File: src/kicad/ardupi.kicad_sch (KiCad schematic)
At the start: 60 parts

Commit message: +adc
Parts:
- removed U (x8): (no value), symbol Device:R_Small
- added J: 6_PIN_SERIAL_TARGET, 1X06, symbol SparkFun-Connectors:6_PIN_SERIAL_TARGET
- added U (x12): (no value), symbol Device:R_Small
- added U: (no value), symbol Device:C_Small
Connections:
- net GND: now also U.3 (GND), J.CTS (5), J.GND (6), U.1, U.1
- net PWM10: now also U.1
- net PWM11: now also U.1
- net PWM12: now also U.1
- net PWM13: now also U.1
- net PWM14: now also U.1
- net PWM15: now also U.1
- net PWM16: now also U.1
- net PWM9: now also U.1
- net at U.1: now also U.2 (x2)
- net at U.4: now also U.2 (x2)
- net at U.7: now also U.2 (x2)
- net at U.10: now also U.2
- net at U.1 (ADDR): now also U.2
- net at U.10 (SCL): now also U.1
- net at U.2 (ALERT/RDY): now also U.1
- net AIO0: now reaches U.4 (AIN0)
- net AIO0: now also J.VCC (4)
- net AIO1: now reaches U.5 (AIN1)
- net AIO1: now also J.TXO (3)
- net AIO2: now reaches U.6 (AIN2)
- net AIO2: now also J.RXI (2)
- net AIO3: now reaches U.7 (AIN3)
- net AIO3: now also J.DTR (1)
- net VDD: now reaches U.8 (VDD)
- net VDD: now also U.2, U.2, U.2
- net at U.9 (SDA): now also U.1
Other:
- note added: "ADC1"
- note added: "MPU9250"
- moved on the sheet: J, U

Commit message: fix
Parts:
- removed J (x3): CONN_04POLAR, MOLEX-1X4, symbol SparkFun-Connectors:CONN_04POLAR
- removed J: 6_PIN_SERIAL_TARGET, 1X06, symbol SparkFun-Connectors:6_PIN_SERIAL_TARGET
- removed J: Conn_01x10, symbol Connector_Generic:Conn_01x10
- removed J: CONN_06POLAR, MOLEX-1X6, symbol SparkFun-Connectors:CONN_06POLAR
- removed J: CONN_02POLAR, MOLEX-1X2, symbol SparkFun-Connectors:CONN_02POLAR
- removed J: CONN_05, 1X05, symbol SparkFun-Connectors:CONN_05
- removed U (x4): (no value), symbol Adafruit PCA9685 rev C-eagle-import:HEADER-3X04
- removed U (x22): (no value), symbol Device:R_Small
- removed U: (no value), symbol Device:C_Small
- added C?: 10uF, Capacitor_SMD:C_0402_1005Metric, symbol Device:C_Small
- added J?: Conn_01x02, Connector_JST:JST_EH_B2B-EH-A_1x02_P2.50mm_Vertical, symbol Connector_Generic:Conn_01x02
- added J?: Conn_01x04, symbol Connector_Generic:Conn_01x04
- added J?: Conn_01x06, symbol Connector_Generic:Conn_01x06
- added J? (x2): Conn_01x04, Connector_JST:JST_EH_B4B-EH-A_1x04_P2.50mm_Vertical, symbol Connector_Generic:Conn_01x04
- added J?: Conn_01x05, Connector_JST:JST_EH_B5B-EH-A_1x05_P2.50mm_Vertical, symbol Connector_Generic:Conn_01x05
- added J?: Conn_01x10, symbol Connector_Generic:Conn_01x10
- added J?: Conn_01x05, symbol Connector_Generic:Conn_01x05
- added JP? (x4): PWM-HEADER-3X04, Ardupi:PWM-Header-3x4, symbol Ardupi:PWM-HEADER-3X04
- added R? (x16): 220 Ω, Resistor_SMD:R_0402_1005Metric, symbol Device:R_Small
- added R? (x4): 10KΩ, Resistor_SMD:R_0402_1005Metric, symbol Device:R_Small
- added R? (x2): 470k, Resistor_SMD:R_0402_1005Metric, symbol Device:R_Small
- BMP280: renamed from U; value (none) -> BMP280; footprint (none) -> Package_LGA:Bosch_LGA-8_2x2.5mm_P0.65mm_ClockwisePinNumbering
- C1, C3: renamed from U; value (none) -> 0.1uF; footprint (none) -> Capacitor_SMD:C_0402_1005Metric
- C2, C5: renamed from U; value (none) -> 1uF; footprint (none) -> Capacitor_SMD:C_0402_1005Metric
- C4: renamed from U; value (none) -> 0.01uF; footprint (none) -> Capacitor_SMD:C_0402_1005Metric
- C_PCA1: renamed from U; value (none) -> 10uF; footprint (none) -> Capacitor_SMD:CP_Elec_8x5.4
- H1, H2, H3, H4: renamed from U; value (none) -> MountingHole; footprint (none) -> lib:MountingHole_2.7mm_M2.5_uHAT_RPi
- J1: renamed from U; value (none) -> GPIO_CONNECTOR; footprint (none) -> lib:PinSocket_2x20_P2.54mm_Vertical_Centered_Anchor
- R1, R3, R4, R5: renamed from U; value (none) -> 10K; footprint (none) -> Resistor_SMD:R_0402_1005Metric
- R2, R6, R7: renamed from U; value (none) -> 10k; footprint (none) -> Resistor_SMD:R_0402_1005Metric
- R24, R25, R27, R29, R30: renamed from U; value (none) -> 4.7KΩ; footprint (none) -> Resistor_SMD:R_0402_1005Metric
- R26, R28, R31: renamed from U; value (none) -> 10KΩ; footprint (none) -> Resistor_SMD:R_0402_1005Metric
- U1: renamed from U; value (none) -> MPU-9250; footprint (none) -> Sensor_Motion:InvenSense_QFN-24_3x3mm_P0.4mm
- U2: renamed from U; value (none) -> ULN2803ADW; footprint (none) -> uln2803ADW:ULN2803ADW
- U4: renamed from U; value (none) -> PCA9685BS; footprint (none) -> Package_DFN_QFN:QFN-28-1EP_6x6mm_P0.65mm_EP4.25x4.25mm
- U6: renamed from U; value (none) -> ADS1115IRUGR; footprint (none) -> ADS1115IRUGR:ADS1115IRUGR
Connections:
- net +5V: now also J?.1 (Pin_1), J?.1 (Pin_1), J?.1 (Pin_1), J?.2 (Pin_2), J?.2 (Pin_2), JP?.11, JP?.11, JP?.11, JP?.11, JP?.2, JP?.2, JP?.2, JP?.2, JP?.5, JP?.5, JP?.5, JP?.5, JP?.8, JP?.8, JP?.8, JP?.8, R?.1
- net AIO0: now also J?.4 (Pin_4); no longer U6.4 (AIN0)
- net AIO1: now also U6.4 (AIN0), J?.3 (Pin_3); no longer U6.5 (AIN1)
- net AIO2: now also U6.5 (AIN1), J?.2 (Pin_2); no longer U6.6 (AIN2)
- net AIO3: now also U6.6 (AIN2), J?.1 (Pin_1)
- net BUZZER_OUT: now also J?.1 (Pin_1)
- net GND: now also C?.2, J?.1 (Pin_1), J?.1 (Pin_1), J?.2 (Pin_2), J?.4 (Pin_4), J?.4 (Pin_4), J?.5 (Pin_5), J?.6 (Pin_6), JP?.12, JP?.12, JP?.12, JP?.12, JP?.3, JP?.3, JP?.3, JP?.3, JP?.6, JP?.6, JP?.6, JP?.6, JP?.9, JP?.9, JP?.9, JP?.9, R?.1
- net MISO: now also J?.4 (Pin_4)
- net MOSI: now also J?.3 (Pin_3)
- net PCA_EN: now also R?.1
- net PWM1: now also R?.2
- net PWM10: now also R?.2
- net PWM11: now also R?.2
- net PWM12: now also R?.2
- net PWM13: now also R?.2
- net PWM14: now also R?.2
- net PWM15: now also R?.2
- net PWM16: now also R?.2
- net PWM2: now also R?.2
- net PWM3: now also R?.2
- net PWM4: now also R?.2
- net PWM5: now also R?.2
- net PWM6: now also R?.2
- net PWM7: now also R?.2
- net PWM8: now also R?.2
- net PWM9: now also R?.2
- net RC1: now also J?.3 (Pin_3)
- net RC2: now also J?.4 (Pin_4)
- net RC3: now also J?.5 (Pin_5)
- net RC4: now also J?.6 (Pin_6)
- net RC5: now also J?.7 (Pin_7)
- net RC6: now also J?.8 (Pin_8)
- net RC7: now also J?.9 (Pin_9)
- net RC8: now also J?.10 (Pin_10)
- net RX: now also J?.4 (Pin_4)
- net SCL: now also J?.3 (Pin_3), J?.3 (Pin_3)
- net SCLK: now also J?.5 (Pin_5)
- net SDA: now also J?.2 (Pin_2), J?.2 (Pin_2)
- net SRVO_EN: now also J?.1 (Pin_1)
- net TX: now also J?.3 (Pin_3)
- net VDD: now also R?.2, R?.2, R?.2; no longer U6.8 (VDD)
- net V_EXT: now also J?.5 (Pin_5)
- net at U6.1 (ADDR): now also R?.2
- net at U6.9 (SDA): now also R?.1
- net at U6.2 (ALERT/RDY): now also R?.1
- net at U6.10 (SCL): now also R?.1
- net LED_1 renamed LED1
- net LED_1_OUT renamed LED1_OUT
- net LED1_OUT: now also J?.2 (Pin_2)
- net LED_2 renamed LED2
- net LED_2_OUT renamed LED2_OUT
- net LED2_OUT: now also J?.3 (Pin_3)
- net LED_3 renamed LED3
- net LED_3_OUT renamed LED3_OUT
- net LED3_OUT: now also J?.4 (Pin_4)
- new net: J?.2 (Pin_2), R?.2, R?.2
- new net: JP?.1, R?.1 (x4)
- new net: JP?.10, R?.1 (x4)
- new net: JP?.7, R?.1 (x4)
- new net: JP?.4, R?.1 (x4)
- new net: C?.1, U6.8 (VDD)
- no-connect marks 29 -> 28
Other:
- note added: "ADC"
- note added: "I2C"
- note added: "RC"
- note added: "SERIAL"
- note added: "SPI"
- note removed: "ADC1"
- note removed: "I2C1"
- note removed: "RC In"
- note removed: "SPI1"
- note removed: "Serial1"
- moved on the sheet: C1, C2, C3, C4, C5, C_PCA1, J1, R1, R2, U1, U2, U4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

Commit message: clean layout
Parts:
- removed JP? (x2): PWM-HEADER-3X04, Ardupi:PWM-Header-3x4, symbol Ardupi:PWM-HEADER-3X04
- removed R? (x8): 220 Ω, Resistor_SMD:R_0402_1005Metric, symbol Device:R_Small
- J2: renamed from J?; footprint (none) -> Connector_JST:JST_EH_B10B-EH-A_1x10_P2.50mm_Vertical
- J3: renamed from J?; footprint (none) -> Connector_JST:JST_EH_B5B-EH-A_1x05_P2.50mm_Vertical
- J4: renamed from J?; footprint (none) -> Connector_JST:JST_EH_B4B-EH-A_1x04_P2.50mm_Vertical
- J6: renamed from J?; footprint (none) -> Connector_JST:JST_EH_B6B-EH-A_1x06_P2.50mm_Vertical
- U6: footprint ADS1115IRUGR:ADS1115IRUGR -> Ardupi:ADS1115IRUGR
- gave numbers to parts that had none: 21
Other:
- moved on the sheet: BMP280, C1, C2, C3, C4, C5, C6, C_PCA1, JP1, JP2, R1, R2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

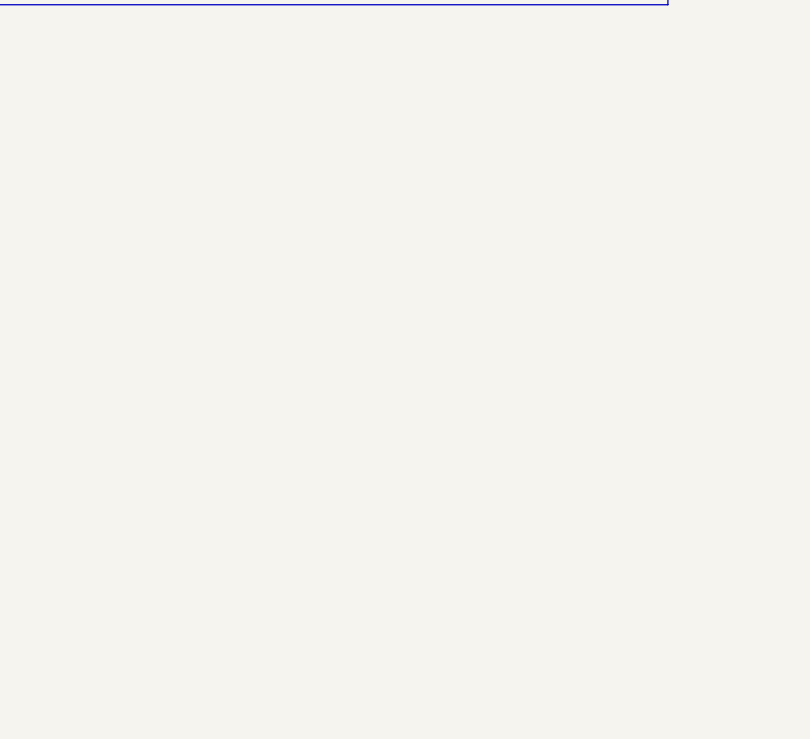
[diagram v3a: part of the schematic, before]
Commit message: +3x8 PWM header
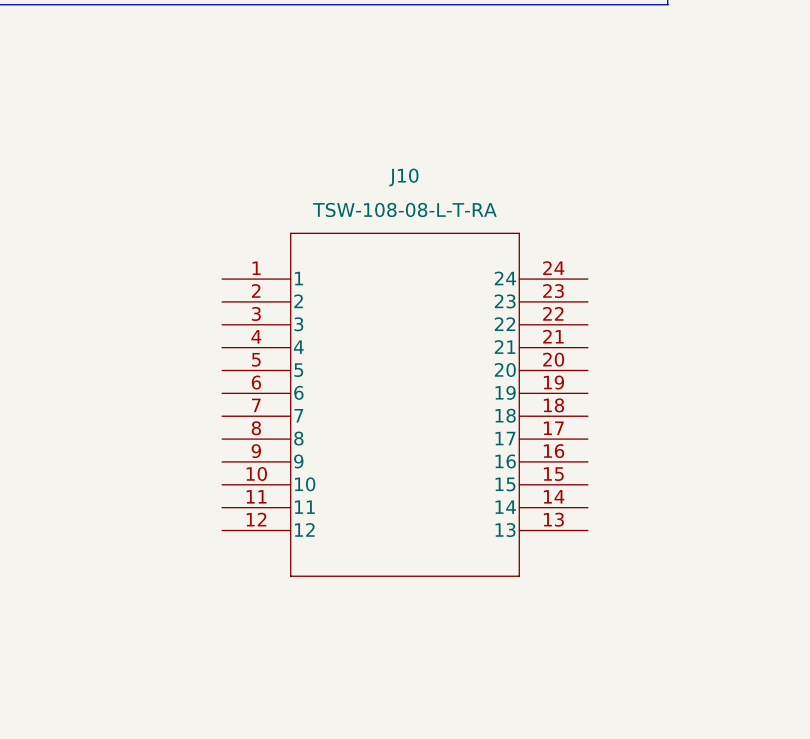
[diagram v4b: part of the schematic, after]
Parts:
- added J10: TSW-108-08-L-T-RA, Ardupi:TSW-108-08-L-T-RA, symbol Ardupi:TSW-108-08-L-T-RA

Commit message: elec: ADS1115
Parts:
- removed R34: 10KΩ, Resistor_SMD:R_0402_1005Metric, symbol Device:R_Small
- added C?: 0.1uf, Capacitor_SMD:C_0402_1005Metric, symbol Device:C_Small
- added R?: 10KΩ, Resistor_SMD:R_0402_1005Metric, symbol Device:R_Small
- C6: value 10uF -> 1uF
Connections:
- net AIO0: now also U6.4 (AIN0)
- net AIO1: now also U6.5 (AIN1); no longer U6.4 (AIN0)
- net AIO2: now also U6.6 (AIN2); no longer U6.5 (AIN1)
- net AIO3: no longer U6.6 (AIN2)
- net GND: now also C?.2
- net SCL1: now also R36.1, U6.10 (SCL)
- net SDA1: now also R37.1, U6.9 (SDA)
- net VDD: now also C6.1, U6.8 (VDD), C?.1, R?.2
- net at U6.1 (ADDR): now also R?.1

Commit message: elec: assign GPIOs and correct some pin labels
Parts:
- removed R1: 10K, Resistor_SMD:R_0402_1005Metric, symbol Device:R_Small
- added R? (x2): 10k, Resistor_SMD:R_0402_1005Metric, symbol Device:R_Small
- R8: value 470k -> 10K
- R9: value 470k -> 460
- gave numbers to parts that had none: 2
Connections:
- net GPIO13 is gone; now on net RC3: J1.33 (Pin_33)
- net GPIO16 is gone; now on net RC8: J1.36 (Pin_36)
- net GPIO17_GEN0 is gone; now on net SRVO_EN: J1.11 (Pin_11)
- net GPIO19 is gone; now on net RC4: J1.35 (Pin_35)
- net GPIO20 is gone; now on net RC7: J1.38 (Pin_38)
- net GPIO21 is gone; now on net RC6: J1.40 (Pin_40)
- net GPIO22_GEN3 is gone; now on net LED2: J1.15 (Pin_15)
- net GPIO26 is gone; now on net RC5: J1.37 (Pin_37)
- net GPIO27_GEN2 is gone; now on net LED1: J1.13 (Pin_13)
- net GPIO4_GPIO_GCLK is gone; now on net LED3: J1.7 (Pin_7)
- net GPIO5 is gone; now on net RC1: J1.29 (Pin_29)
- net GPIO6 is gone; now on net RC2: J1.31 (Pin_31)
- net VDD is gone; now on net +5V: C6.1, C7.1, R18.2, R35.2, R36.2, R37.2, U6.8 (VDD)
- net +5V: now also R?.1, R?.1; no longer JP1.11, JP1.2, JP1.5, JP1.8, JP2.11, JP2.2, JP2.5, JP2.8
- net PCA_EN: now also U4.20 (~{OE})
- net SCL1: now also R?.2
- net SDA1: now also R?.2
- net V_EXT: now also JP1.11, JP1.2, JP1.5, JP1.8, JP2.11, JP2.2, JP2.5, JP2.8
- net GPIO12 renamed Buzzer
- net GPIO23_GEN4 renamed GPIO23
- net GPIO24_GEN5 renamed GPIO24

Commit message: +HAT ID EEPROM +standard rpi-4b footprint +clean up of schematic
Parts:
- removed JP1, JP2: PWM-HEADER-3X04, Ardupi:PWM-Header-3x4, symbol Ardupi:PWM-HEADER-3X04
- removed R10, R11, R12: 220 Ω, Resistor_SMD:R_0402_1005Metric, symbol Device:R_Small
- added C1: 100n, symbol Device:C_Small
- added JP1: ID_WP, symbol Jumper:SolderJumper_2_Open
- added R1, R2: 3.9k, symbol Device:R_Small
- added R18, R19, R20: 220 Ω, Resistor_SMD:R_0402_1005Metric, symbol Device:R_Small
- added U1: CAT24C256, symbol Memory_EEPROM:CAT24C256
- gave numbers to parts that had none: 2
- renumbered BMP280 to BMP1, C1 to C2, C2 to C3, C6 to C4, C7 to C5, C3 to C6, C4 to C7, C5 to C8, J9 to J10, J10 to J11, J1 to J5, J5 to J6, J6 to J7, J7 to J8, J8 to J9, R7 to R10, R8 to R11, R9 to R12, R24 to R21, R25 to R22, R26 to R23, R27 to R24, R35 to R25, R28 to R26, R18 to R27, R29 to R28, R30 to R29, R31 to R30, R36 to R31, R37 to R32, R2 to R5, R3 to R6, R4 to R7, R5 to R8, R6 to R9, U4 to U3, U6 to U4, U1 to U5
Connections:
- net +3.3V is gone; now on net GND: BMP1.6 (VDDIO), BMP1.8 (VDD), C2.1, C3.1, C7.1, C8.1, R21.1, R22.1, R24.1, R26.2, R28.2, R29.2, U5.13 (VDD), U5.8 (VDDIO)
- net Buzzer is gone; now on net BUZZER: J5.32 (Pin_32)
- net +3V3: now also C1.1, JP1.2 (B), R1.1, R2.1, U1.8 (VCC)
- net GND: now also J11.12, J11.15, J11.18, J11.21, J11.24, J11.3, J11.6, J11.9, C1.2, U1.4 (GND)
- net PWM1: now also R13.2
- net PWM2: now also R14.2
- net PWM3: now also R15.2
- net PWM4: now also R16.2; no longer R13.2
- net PWM5: now also R20.1; no longer R14.2
- net PWM6: now also R19.1; no longer R15.2
- net PWM7: now also R18.1; no longer R16.2
- net PWM8: now also R17.1; no longer R17.2
- net V_EXT: now also J11.11, J11.14, J11.17, J11.2, J11.20, J11.23, J11.5, J11.8
- net at R14.1: now also J11.4
- net at R15.1: now also J11.7
- net at R16.1: now also J11.10
- net at R13.1: now also J11.1
- net at J11.13: now also R20.2
- net at J11.16: now also R19.2
- net at J11.19: now also R18.2
- net at J11.22: now also R17.2
- net ID_SC renamed ID_SCL
- net ID_SCL: now also R2.2, U1.6 (SCL)
- net ID_SD renamed ID_SDA
- net ID_SDA: now also R1.2, U1.5 (SDA)
- new net: JP1.1 (A), U1.7 (WP)
- no-connect marks 28 -> 3
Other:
- note added: "BMP280 Barometer"
- note added: "DISARM"
- note added: "HAT ID EEPROM"
- note added: "ID_SD and ID_SC PINS: These pins are reserved for HAT ID EEPROM. At boot time this I2C interface will be interrogated to look for an EEPROM that identifes the attached board and allows automagic setup of the GPIOs (and optionally, Linux drivers). Bridging JP1 enables write protection. DO NOT USE these pins for anything other than attaching an I2C ID EEPROM. Leave unconnected if ID EEPROM not requ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"
- note added: "MPU9250 IMU"
- note added: "PCA9685 PWM"
- note added: "ULN2803 LED,BUZZER"
- note added: "ads111x ADC"
- note removed: "BMP280"
- note removed: "Disarm"
- note removed: "MPU9250"
- note removed: "PCA9685"
- note removed: "Template"
- note removed: "ULN2803"
- note removed: "ads111x"
- moved on the sheet: BMP1, C2, C3, C4, C5, C6, C7, C8, C_PCA1, H1, H2, H3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
